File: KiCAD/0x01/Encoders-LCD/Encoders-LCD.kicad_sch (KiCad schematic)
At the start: 35 parts, among them J1 Conn_B1, J2 Conn_B4, J3 Conn_B3, SW1 RotaryEncoder_Switch, SW2 RotaryEncoder_Switch, SW3 RotaryEncoder_Switch, SW4 SW_Push_LED, U1 ST7789, U2 CD74HC4067M, U3 ST7789

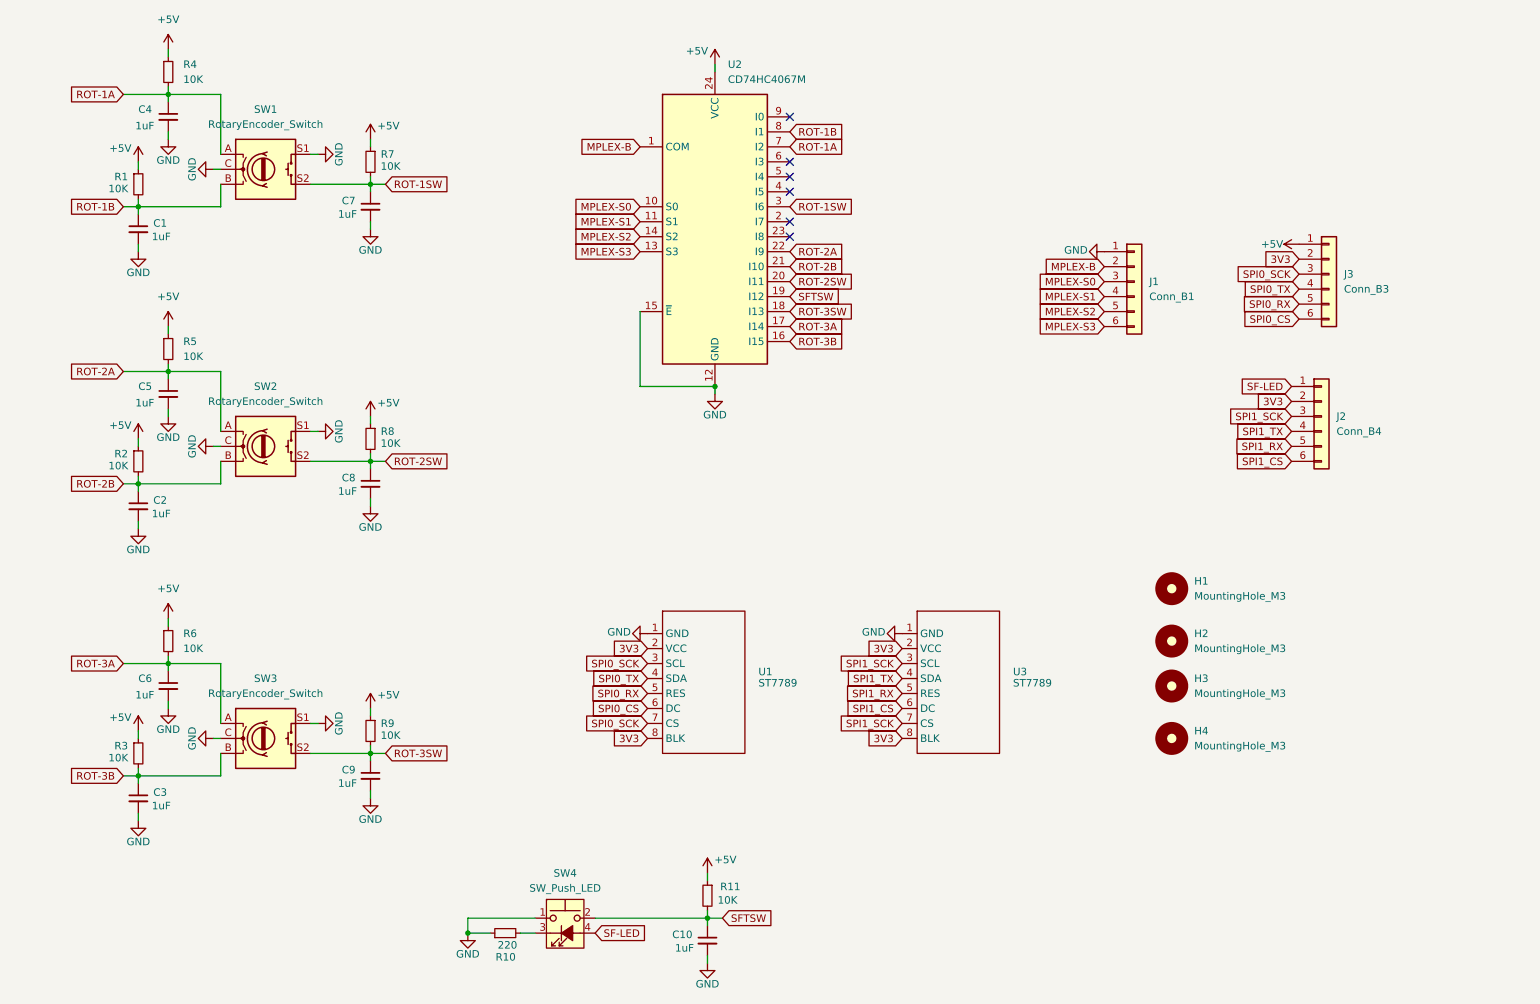
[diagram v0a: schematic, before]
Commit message: fix lcd encoders
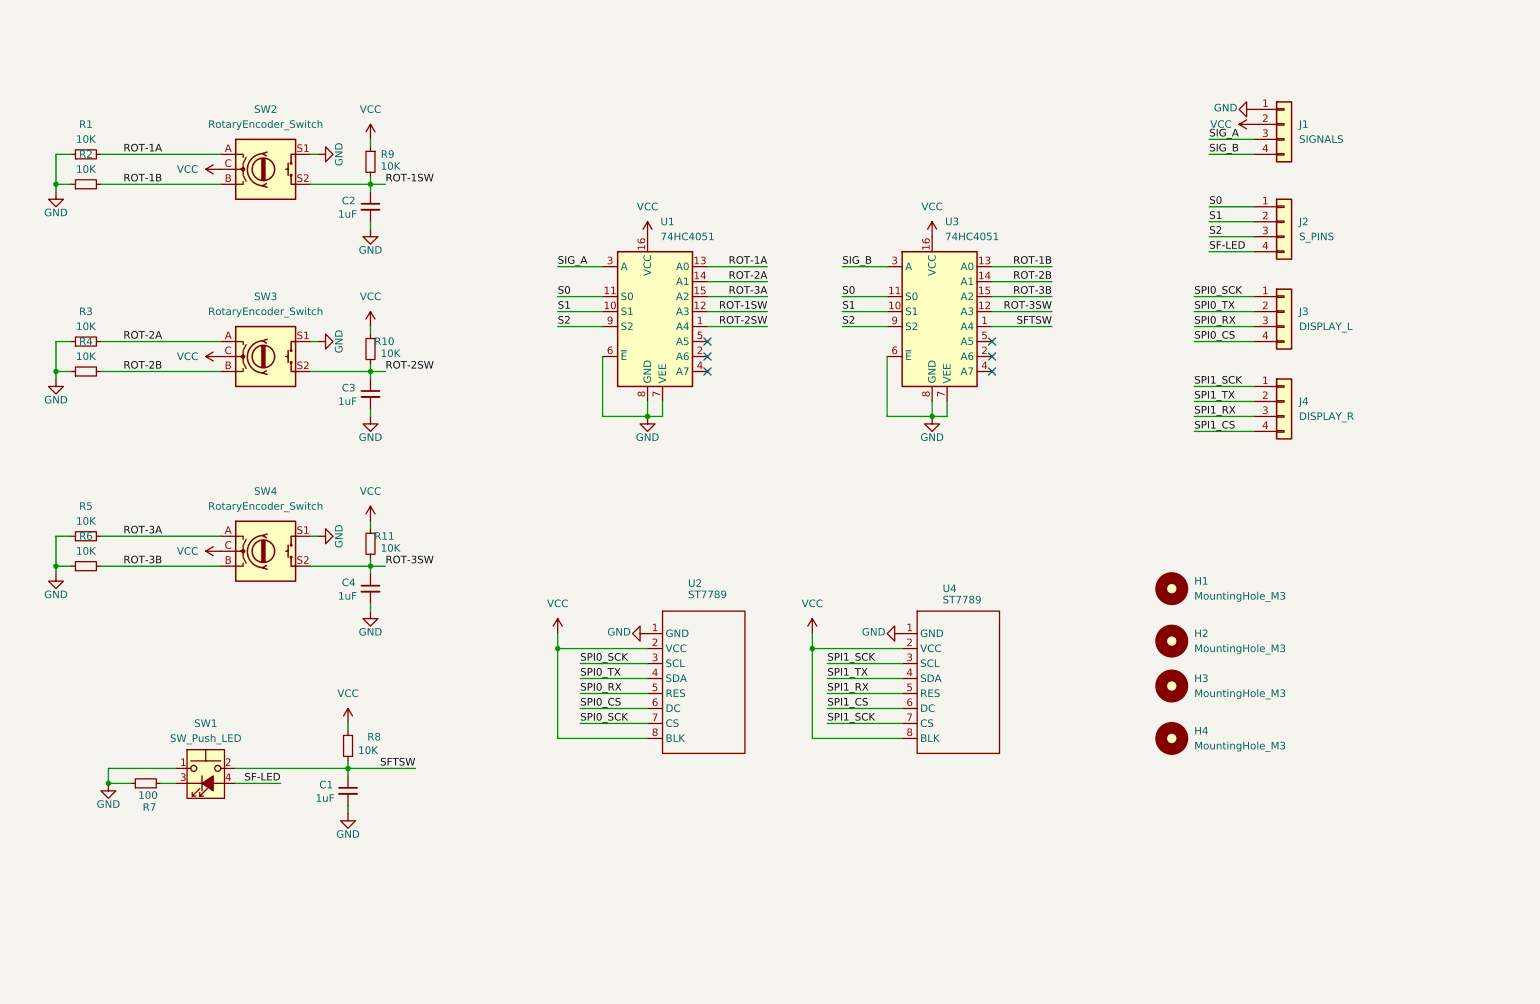
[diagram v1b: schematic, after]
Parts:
- removed C1, C2, C5, C6, C8, C9: 1uF, Capacitor_SMD:C_1206_3216Metric_Pad1.33x1.80mm_HandSolder, symbol Device:C_Small
- removed J1: Conn_B1, Connector_PinHeader_2.54mm:PinHeader_1x06_P2.54mm_Vertical, symbol Connector_Generic:Conn_01x06
- removed J2: Conn_B4, Connector_PinHeader_2.54mm:PinHeader_1x06_P2.54mm_Vertical, symbol Connector_Generic:Conn_01x06
- removed J3: Conn_B3, Connector_PinHeader_2.54mm:PinHeader_1x06_P2.54mm_Vertical, symbol Connector_Generic:Conn_01x06
- removed R8, R9: 10K, PCM_Resistor_SMD_AKL:R_1206_3216Metric_Pad1.30x1.75mm_HandSolder, symbol Device:R_Small
- removed SW2: RotaryEncoder_Switch, Rotary_Encoder:RotaryEncoder_Alps_EC11E-Switch_Vertical_H20mm_CircularMountingHoles, symbol Device:RotaryEncoder_Switch
- removed U2: CD74HC4067M, Package_SO:SOIC-24W_7.5x15.4mm_P1.27mm, symbol 74xx:CD74HC4067M
- added J1: SIGNALS, Connector_Molex:Molex_KK-254_AE-6410-04A_1x04_P2.54mm_Vertical, symbol Connector_Generic:Conn_01x04
- added J2: S_PINS, Connector_Molex:Molex_KK-254_AE-6410-04A_1x04_P2.54mm_Vertical, symbol Connector_Generic:Conn_01x04
- added J3: DISPLAY_L, Connector_Molex:Molex_KK-254_AE-6410-04A_1x04_P2.54mm_Vertical, symbol Connector_Generic:Conn_01x04
- added J4: DISPLAY_R, Connector_Molex:Molex_KK-254_AE-6410-04A_1x04_P2.54mm_Vertical, symbol Connector_Generic:Conn_01x04
- added R10, R11: 10K, PCM_Resistor_SMD_AKL:R_1206_3216Metric_Pad1.30x1.75mm_HandSolder, symbol Device:R_Small
- added SW4: RotaryEncoder_Switch, Rotary_Encoder:RotaryEncoder_Alps_EC11E-Switch_Vertical_H20mm_CircularMountingHoles, symbol Device:RotaryEncoder_Switch
- added U1, U3: 74HC4051, Package_SO:SOP-16_4.4x10.4mm_P1.27mm, symbol 74xx:74HC4051
- R7: renamed from R10; value 220 -> 100
- SW1: renamed from SW4; footprint led-switch:SW_PUSH_6mm_LED -> led-sw:led switch
- renumbered C10 to C1, C7 to C2, R11 to R8, R7 to R9, SW1 to SW2, U1 to U2, U3 to U4
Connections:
- net GND: now also R1.1, R2.1, R3.1, R4.1, R5.1, R6.1, J1.1 (Pin_1), SW4.S1, U1.6 (~{E}), U1.7 (VEE), U1.8 (GND), U3.6 (~{E}), U3.7 (VEE), U3.8 (GND); no longer SW2.C, SW3.C
- net ROT-1A: now also R1.2, U1.13 (A0); no longer C4.1, R4.2
- net ROT-1B: now also R2.2, U3.13 (A0); no longer R1.2
- net ROT-1SW: now also U1.12 (A3)
- net ROT-2A: now also R3.2, SW3.A, U1.14 (A1); no longer R5.2
- net ROT-2B: now also R4.2, SW3.B, U3.14 (A1); no longer R2.2
- net ROT-2SW: now also C3.1, SW3.S2, R10.2, U1.1 (A4)
- net ROT-3A: now also R5.2, SW4.A, U1.15 (A2); no longer R6.2, SW3.A
- net ROT-3B: now also R6.2, SW4.B, U3.15 (A2); no longer C3.1, R3.2, SW3.B
- net ROT-3SW: now also C4.1, R11.2, SW4.S2, U3.12 (A3); no longer SW3.S2
- net SF-LED: now also J2.4 (Pin_4)
- net SFTSW: now also U3.1 (A4)
- net SPI0_CS: now also J3.4 (Pin_4)
- net SPI0_RX: now also J3.3 (Pin_3)
- net SPI0_SCK: now also J3.1 (Pin_1)
- net SPI0_TX: now also J3.2 (Pin_2)
- net SPI1_CS: now also J4.4 (Pin_4)
- net SPI1_RX: now also J4.3 (Pin_3)
- net SPI1_SCK: now also J4.1 (Pin_1)
- net SPI1_TX: now also J4.2 (Pin_2)
- removed net +5V: R1.1, R2.1, R3.1, R4.1, R5.1, R6.1, R8.1, R9.1
- net 3V3 renamed VCC
- net VCC: now also R8.1, R9.1, SW2.C, SW3.C, J1.2 (Pin_2), R10.1, R11.1, SW4.C, U1.16 (VCC), U3.16 (VCC)
- new net S0: J2.1 (Pin_1), U1.11 (S0), U3.11 (S0)
- new net S1: J2.2 (Pin_2), U1.10 (S1), U3.10 (S1)
- new net S2: J2.3 (Pin_3), U1.9 (S2), U3.9 (S2)
- new net SIG_A: J1.3 (Pin_3), U1.3 (A)
- new net SIG_B: J1.4 (Pin_4), U3.3 (A)
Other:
- moved on the sheet: C1, R7, R8, SW1

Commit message: 7789
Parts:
- removed C4: 1uF, Capacitor_SMD:C_1206_3216Metric_Pad1.33x1.80mm_HandSolder, symbol Device:C_Small
- removed J1: SIGNALS, Connector_Molex:Molex_KK-254_AE-6410-04A_1x04_P2.54mm_Vertical, symbol Connector_Generic:Conn_01x04
- removed J2: S_PINS, Connector_Molex:Molex_KK-254_AE-6410-04A_1x04_P2.54mm_Vertical, symbol Connector_Generic:Conn_01x04
- removed J3: DISPLAY_L, Connector_Molex:Molex_KK-254_AE-6410-04A_1x04_P2.54mm_Vertical, symbol Connector_Generic:Conn_01x04
- removed J4: DISPLAY_R, Connector_Molex:Molex_KK-254_AE-6410-04A_1x04_P2.54mm_Vertical, symbol Connector_Generic:Conn_01x04
- removed R10, R11, R3, R4, R5, R6, R9: 10K, PCM_Resistor_SMD_AKL:R_1206_3216Metric_Pad1.30x1.75mm_HandSolder, symbol Device:R_Small
- removed U1, U3: 74HC4051, Package_SO:SOP-16_4.4x10.4mm_P1.27mm, symbol 74xx:74HC4051
- removed U2, U4: ST7789, Display-oled:1.14 7789, symbol r3m1xxx_Library:ST7789-oled
- added J1: Conn_01x06, Connector_Hirose:Hirose_DF13-06P-1.25DSA_1x06_P1.25mm_Vertical, symbol Connector_Generic:Conn_01x06
- added U1: UC1, Package_SO:SOIC-8_3.9x4.9mm_P1.27mm, symbol MCU_Microchip_ATtiny:ATtiny412-SS
- added U2: UC2, Package_SO:SOIC-8_3.9x4.9mm_P1.27mm, symbol MCU_Microchip_ATtiny:ATtiny412-SS
- added U3: UC3, Package_SO:SOIC-8_3.9x4.9mm_P1.27mm, symbol MCU_Microchip_ATtiny:ATtiny412-SS
- C2: value 1uF -> 100nF
- C3: value 1uF -> 10uF
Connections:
- net ROT-3SW is gone; now on net GND: SW4.S2
- net GND: now also SW2.C, SW2.S2, SW3.C, SW3.S2, SW4.C, J1.1 (Pin_1), U1.8 (GND), U2.8 (GND), U3.8 (GND); no longer R1.1, R2.1, SW2.S1, SW3.S1, SW4.S1
- net SFTSW: now also J1.5 (Pin_5)
- net VCC: now also C2.1, C3.1, R1.1, R2.1, J1.2 (Pin_2), U1.1 (VCC), U2.1 (VCC), U3.1 (VCC); no longer SW2.C, SW3.C, SW4.C
- net ROT-1A renamed A1
- net A1: now also U1.3 (PA7); no longer R1.2
- net ROT-1B renamed B1
- net B1: now also U1.2 (PA6); no longer R2.2
- removed net ROT-1SW: C2.1, SW2.S2
- net ROT-2A renamed A2
- net A2: now also U2.3 (PA7)
- net ROT-2B renamed B2
- net B2: now also U2.2 (PA6)
- removed net ROT-2SW: C3.1, SW3.S2
- net ROT-3A renamed A3
- net A3: now also U3.3 (PA7)
- net ROT-3B renamed B3
- net B3: now also U3.2 (PA6)
- net SF-LED renamed SFTLED
- net SFTLED: now also J1.6 (Pin_6)
- new net SCL: J1.3 (Pin_3), R2.2, U1.5 (PA2), U2.5 (PA2), U3.5 (PA2)
- new net SDA: J1.4 (Pin_4), R1.2, U1.4 (PA1), U2.4 (PA1), U3.4 (PA1)
- new net SW1: SW2.S1, U1.7 (PA3)
- new net SW2: SW3.S1, U2.7 (PA3)
- new net SW3: SW4.S1, U3.7 (PA3)
- no-connect marks 6 -> 3
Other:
- moved on the sheet: C1, C2, R7, R8, SW1, SW2

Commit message: lcd encoders
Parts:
- removed J1: Conn_01x06, Connector_Hirose:Hirose_DF13-06P-1.25DSA_1x06_P1.25mm_Vertical, symbol Connector_Generic:Conn_01x06
- added J1: I2C_Conn, Connector_Hirose:Hirose_DF13-04P-1.25DS_1x04_P1.25mm_Horizontal, symbol Connector_Generic:Conn_01x04
- added J2: Btn_conn, Connector_Hirose:Hirose_DF13-04P-1.25DS_1x04_P1.25mm_Horizontal, symbol Connector_Generic:Conn_01x04
- added J3: DSP-L, Connector_PinHeader_2.54mm:PinHeader_1x04_P2.54mm_Vertical, symbol Connector_Generic:Conn_01x04
- added J4: DSP-R, Connector_PinHeader_2.54mm:PinHeader_1x04_P2.54mm_Vertical, symbol Connector_Generic:Conn_01x04
- C1, C2, C3: footprint Capacitor_SMD:C_1206_3216Metric_Pad1.33x1.80mm_HandSolder -> Capacitor_SMD:C_0805_2012Metric_Pad1.18x1.45mm_HandSolder
- R1: renamed from R7; footprint PCM_Resistor_SMD_AKL:R_1206_3216Metric_Pad1.30x1.75mm_HandSolder -> PCM_Resistor_SMD_AKL:R_0805_2012Metric_Pad1.20x1.40mm_HandSolder
- R2: renamed from R8; footprint PCM_Resistor_SMD_AKL:R_1206_3216Metric_Pad1.30x1.75mm_HandSolder -> PCM_Resistor_SMD_AKL:R_0805_2012Metric_Pad1.20x1.40mm_HandSolder
- R3: renamed from R1; footprint PCM_Resistor_SMD_AKL:R_1206_3216Metric_Pad1.30x1.75mm_HandSolder -> PCM_Resistor_SMD_AKL:R_0805_2012Metric_Pad1.20x1.40mm_HandSolder
- R4: renamed from R2; footprint PCM_Resistor_SMD_AKL:R_1206_3216Metric_Pad1.30x1.75mm_HandSolder -> PCM_Resistor_SMD_AKL:R_0805_2012Metric_Pad1.20x1.40mm_HandSolder
- SW2, SW3, SW4: footprint Rotary_Encoder:RotaryEncoder_Alps_EC11E-Switch_Vertical_H20mm_CircularMountingHoles -> Display-oled:self-RotaryEncoder_Alps_EC11E-Switch_Vertical_H20mm_CircularMountingHoles
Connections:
- net GND: now also J1.1 (Pin_1), J2.1 (Pin_1), J3.1 (Pin_1), J4.1 (Pin_1)
- net SCL: now also J1.3 (Pin_3), J3.3 (Pin_3), J4.3 (Pin_3)
- net SDA: now also J1.4 (Pin_4), J3.4 (Pin_4), J4.4 (Pin_4)
- net SFTLED: now also J2.4 (Pin_4)
- net SFTSW: now also J2.3 (Pin_3)
- net VCC: now also J1.2 (Pin_2), J2.2 (Pin_2), J3.2 (Pin_2), J4.2 (Pin_2)
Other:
- moved on the sheet: C2, C3, H1, H2, H3, H4, R3, R4
